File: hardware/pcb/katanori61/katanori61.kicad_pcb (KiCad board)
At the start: 4 copper layers, 82 x 37.4 mm, 59 parts, among them J1 XIAO RISER, J10 BAT (JST-PH), J13 USB-C, J2 OLED, J4 SPK IN, J5 SPK OUT, J6 BTN2, J7 REED+TOGGLE, K31 G6S-2F DC5, Q1 MMUN2133LT1G, Q2 AO3401A, Q31 SS8050, U1 TPS61090RSAR, U2 MCP73871-2CCI/ML, U3 INA226AIDGSR, U4 AS5600-ASOM

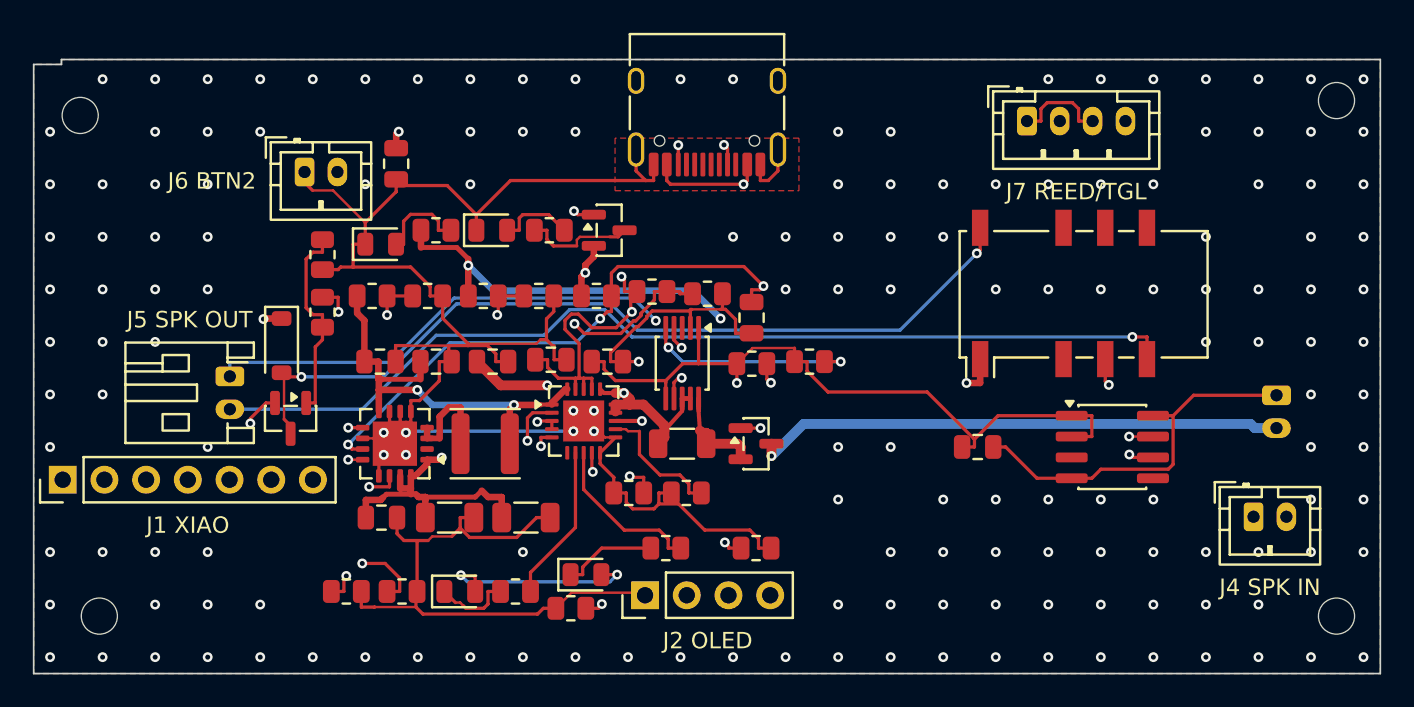
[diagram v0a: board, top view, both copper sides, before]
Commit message: pcb v6.1: R2・R6・R7 を 0603 へ／V5 を 0.8mm の独立した組へ／手はんだの GND にサーマル
外からの指摘 4 件のうち 1〜4 を直す。

1. 足形の食い違い
   Basic で選び直した R2(C23137)・R6(C22961)・R7(C23254) は 0603 なのに
   足形が 0805 のままだった。0805 のパッドの内側の間 0.875 に 0603 の胴 1.6 が
   両端 0.36 ずつ乗るだけで、機械実装で着かないか立つ。

3. V5 が内層を遠回り
   U1 → J1（XIAO）が 57.49mm、うち 57.3mm が In2.Cu。JLCPCB の 4 層は
   内層 0.5oz が既定なので、同じ幅でも抵抗が 2 倍になる。
   0.4mm → 0.8mm の独立した組にして 29.46mm・18.1mΩ（前 141.5mΩ）。
   0.3A で 5.4mV（前 42.5mV）。

4. 電池の道の数字が古い
   gen_pcb.py の「12mm・10mΩ」は J10 を板の真ん中に置いていたときの値。
   実測に入れ替え: J10→Q2 31.16mm/25.5mΩ、Q2→R41 2.18mm/1.8mΩ、
   R41→U2 3.63mm/3.0mΩ、計 36.97mm・30.3mΩ（1A で 30mV）。

2. GND ベタが全パッド直結
   4 層で In1 が全面 GND になり、手はんだの口は 3 層が足に直結してこてで
   温度が逃げる。HAND_SOLDER の貫通 GND だけ thermal relief にした
   （J1-2 / J2-1 / J6-1 / J7-2 / J7-4 / J10-1 の 6 本）。表面実装は直結のまま。
   細いパッドは spoke が 1 本しか立たないので katanori61.kicad_dru を生成し、
   貫通パッドだけ min_resolved_spokes 1 に緩める。

ついでに見つけた不具合
   pad_box() が部品の角度を足しておらず、270° 置きの U3 で縦横が入れ替わって
   いた。ケルビンの線の端が U3 のパッドの 0.335 外に落ちていたのを自動配線が
   繕っていた。
   fab.py の JLC_ROT に R_0603_1608Metric（2 本足・補正 0）を足した。
   gen_case_parts.py の「いまの手書きの表は 9 個」は表を生成に変えた時点で
   嘘になっていたので消した。

検算
   配線 708 本・貫通穴 59 個・未接続 0・回路図との差 0・DRC エラー 0
   （警告は留め穴 4 と USB-C のシルク 2 のみ。starved_thermal は 0）
   模型・STL・ガーバー・BOM・CPL を出し直した。
   レジンの sk_hub 12.02mm³ は以前からの当たり（HEAD で 12.59）。
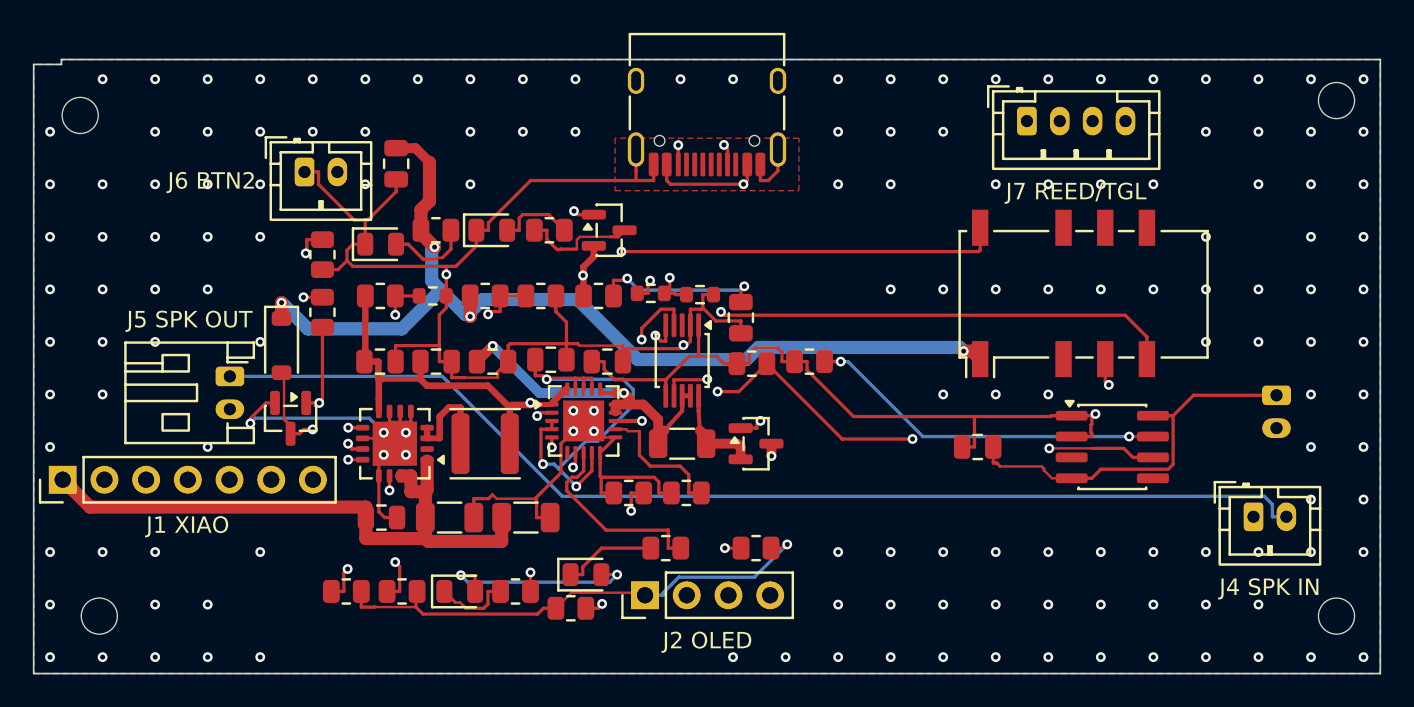
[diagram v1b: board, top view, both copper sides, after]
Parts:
- R2, R6, R7: footprint Resistor_SMD:R_0805_2012Metric -> Resistor_SMD:R_0603_1608Metric
- moved C32 0.65 mm to (83.1, 55.7)
- moved R1 0.50 mm to (61.1, 54.4)
- moved R7 0.46 mm to (80.6, 54.3)
- moved R2 0.31 mm to (64.3, 54.4)
- moved U3 0.16 mm to (79.5, 58.3)
- moved R6 0.13 mm to (77.6, 54.2)
- moved R13 0.12 mm to (74.4, 54.4)
- moved R4 0.12 mm to (70.9, 54.4)
- moved R3 0.12 mm to (67.5, 54.4)
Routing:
- net V33: track 96.2 -> 116.0 mm
- net SPKO: track 60.4 -> 72.3 mm
- net SDA: track 92.6 -> 103.5 mm, vias 3 -> 4
- net SCL: track 95.4 -> 87.5 mm
- net GND: track 305.8 -> 297.9 mm, vias 165 -> 156
- net EN: track 60.3 -> 68.0 mm
- net VPCC: track 21.4 -> 15.1 mm
- net BATG: track 17.2 -> 11.2 mm
- net COL: track 52.3 -> 57.9 mm
- net SPKM: track 73.6 -> 68.3 mm, vias 1 -> 0
- net BASE: track 12.2 -> 16.8 mm, vias 0 -> 2
- net STAT2: track 9.58 -> 13.4 mm, vias 0 -> 2
- net FB: track 20.7 -> 17.4 mm
- net BATRAW: track 32.4 -> 35.0 mm
- net VSYS: track 39.7 -> 37.2 mm, vias 3 -> 2
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
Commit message: pcb v6.1: FB を U1 の足元へ／リレーを AS5600 の横から退けた／長い幹を裏へ
指摘「昇圧の FB が遠い」を直す。板を見たら指摘どおりだった。
  R3 12.42mm / R4 14.32mm・FB はのべ 17.42mm でうち内層 13.21mm・ビア 2 個。
  内層の斜めの区間は L1 の枠を横切り、x 24.73 で FB が y 14.21・SW が y 14.33 ＝ 真下。
  In1 の GND の面は無事（廊下の 2mm 以内の穴 4 個のうち 3 個は GND 自身のビアで面を切らない）。

FB
  R3・R4 を U1 の 14 番の真下（Y 10.65）へ。V5 の出力コンデンサの列を 9.5 → 8.6 に下げて
  1.4mm の廊下を空けた（0805 のパッド 1.45 ＋ すきま 0.15×2 が入らなかったため）。
  ⇒ のべ 3.45mm・全部 F.Cu・ビア 0 個。

🔴 リレー K31 を AS5600 の横から退けた
  前は胴と胴が 3.16mm・芯と芯が 9.47mm で、しかも「筐体の仮置きから前へ 2.0」＝
  電磁石を、磁気で角度を読むセンサの真横へ限界まで寄せていた。
  MEDIATOR-V6-HANDOFF.md 3 章の「設計で潰す手は無い」は誤り。板の 64% には部品の胴が無く、
  留め穴・欠き・縁 0.5 を避けてもリレーが入る場所は 501 通りあった。
  90° 回して X 46.48〜57.18・Y 20.30〜35.60 へ。
    芯と芯 9.47 → 19.81mm（2.09 倍・双極子の場は 1/r³ なので約 9.2 分の 1）
    胴と胴 Y 3.16 → 4.05・X 0 → 6.57
  実機で確かめる項目（つまみを固定して K31 開／閉で AGC と RAW ANGLE を 2 読み）は残る。

長い幹を裏へ（自動配線に任せると内層 0.5oz へ逃げて抵抗が倍になる）
  🔴 2026-09-17 朝に書いた「J10 → Q2 31.16mm・25.5mΩ（B.Cu）」は私の誤り。層を見ずに
     長さだけで計算していた。実際は内層 In2 に 34.27mm で 56.6mΩ だった。
  bat_trunk() … J10 → Q2 を裏へ。56.6 → 26.7mΩ。
    ⚠ 最初 AS5600 の真裏を一直線に通したが、前の帯（Y 9.5）へ下ろした。+2.8mΩ 払って
      センサから 4.7mm 離す。磁気の見積もりは仮定の上の計算で、測った値ではないため。
  v5_trunk() … C6 の足元 → XIAO のライザーを裏へ。64.9 → 20.7mΩ。
  vlipo_link() … R41 → U2。自動配線が引けたり引けなかったりした谷を先に固定。
  R41・U3・Q2 を右へ 1.0。U2 の右の辺と R41 のあいだが 1.595mm しかなく、
  VLIPO 0.6 ＋ PROG1 0.2 ＋ PROG3 0.2 ＋ すきま 0.15×4 ＝ 1.6 に 0.005 足りなかった。

thermal relief の規則の置き場所を直した
  🔴 kicad-cli は katanori61.kicad_dru（カスタム規則）を読まない。わざと壊した規則を
     入れても素通りした。min_resolved_spokes は gen_sch.py が書く .kicad_pro に置く。
  ⇒ .kicad_dru の生成をやめ、ファイルを消した。

検算
  未接続 0・DRC エラー 0（警告は留め穴 4 と USB-C のシルク 2）
  すきまの下限 0.15 を下回る組 0 件（最小 0.152）
  筐体の当たり sk_hub は **レジンもナイロンも 0.00mm³**（以前から残っていたレジンの
  12.02mm³ も消えた）
  ⚠ 板の外は数えていない。電池に最初から付いている尻尾は 26AWG 80mm 往復で 20.6mΩ、
    28AWG なら 34.0mΩ あり、板の道より大きい。実物の線を測るのが先。
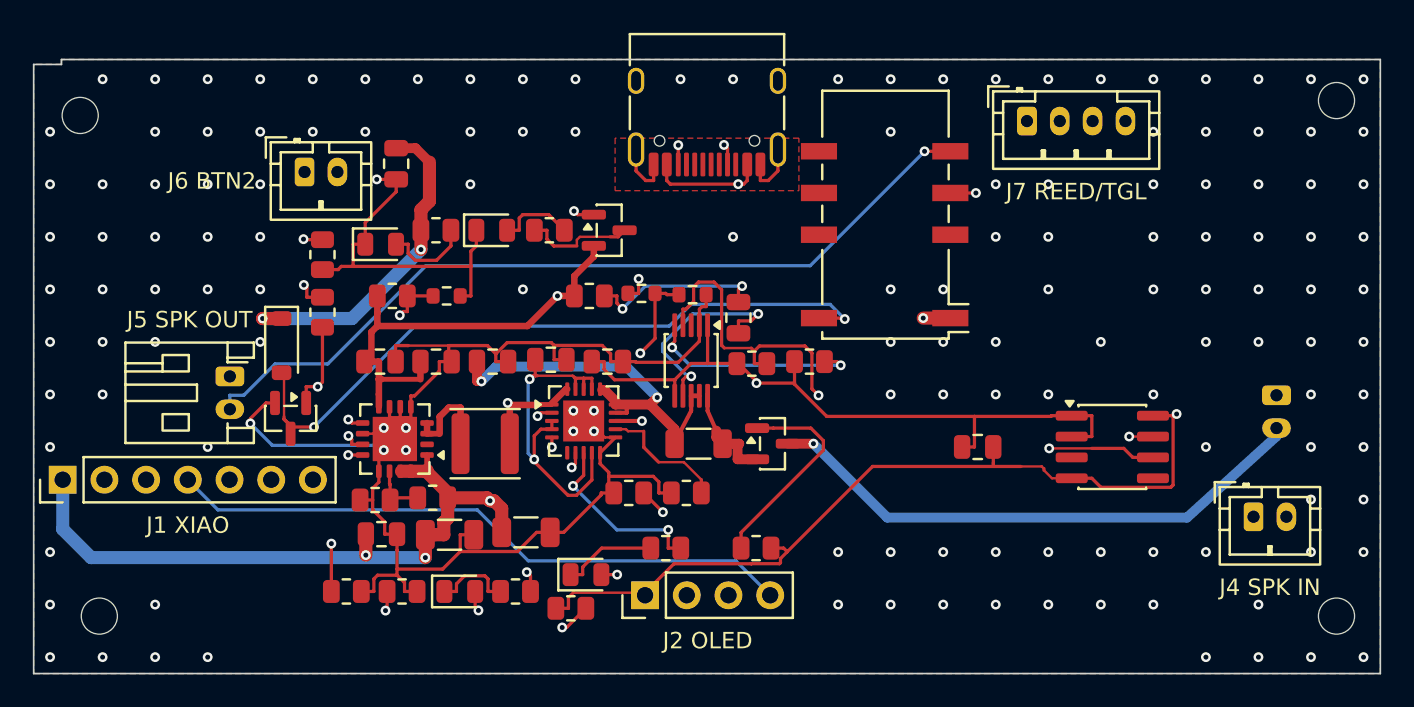
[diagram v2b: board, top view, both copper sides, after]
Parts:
- C4: renamed from C8; value 10uF -> 0.1uF
- C41: renamed from R43; value 10K -> 0.1uF; footprint Resistor_SMD:R_0805_2012Metric -> Capacitor_SMD:C_0805_2012Metric
- C7: renamed from C41; value 0.1uF -> 10uF
- C8: renamed from R42; value 10K -> 10uF; footprint Resistor_SMD:R_0805_2012Metric -> Capacitor_SMD:C_0805_2012Metric
- R16: renamed from C1; value 10uF -> 1.0K; footprint Capacitor_SMD:C_0805_2012Metric -> Resistor_SMD:R_0805_2012Metric
- R17: renamed from C4; value 0.1uF -> 100K; footprint Capacitor_SMD:C_0805_2012Metric -> Resistor_SMD:R_0805_2012Metric
- R2: renamed from R4; value 200K -> 330K; footprint Resistor_SMD:R_0805_2012Metric -> Resistor_SMD:R_0603_1608Metric
- R3: renamed from R17; value 100K -> 1.87M
- R4: renamed from R16; value 1.0K -> 200K
- R42: renamed from R1; value 1.87M -> 10K
- R43: renamed from R2; value 330K -> 10K; footprint Resistor_SMD:R_0603_1608Metric -> Resistor_SMD:R_0805_2012Metric
- moved R43 23.3 mm to (87.3, 58.4)
- moved R42 23.0 mm to (83.7, 58.5)
- moved R17 17.2 mm to (79.8, 66.4)
- moved R16 17.1 mm to (76.2, 66.4)
- moved R4 15.5 mm to (60.8, 66.8), turned to 180 degrees
- moved R3 15.5 mm to (64.3, 66.7), turned to 180 degrees
- moved K31 13.1 mm to (91.8, 49.4), turned to 180 degrees
- moved C41 12.3 mm to (74.9, 58.4)
- moved C8 12.2 mm to (71.5, 58.3)
- moved C4 6.99 mm to (64.5, 58.4)
- moved C7 6.99 mm to (68.0, 58.4)
- moved C1 6.86 mm to (61.1, 58.4)
- moved R2 5.73 mm to (65.2, 54.4)
- moved R1 5.66 mm to (61.8, 54.4)
- moved C6 1.05 mm to (65.3, 68.9)
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- renumbered C7 to C1, R3 to R1
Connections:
- C1 pad 1: VLIPO -> VSYS
- C4 pad 1: VBUS -> VSYS
- C41 pad 2: SCL -> GND
- C7 pad 1: V33 -> VLIPO
- C8 pad 1: V33 -> VBUS
- C8 pad 2: SDA -> GND
- R1 pad 1: V5 -> VSYS
- R1 pad 2: FB -> LBI
- R16 pad 1: VSYS -> GND
- R16 pad 2: GND -> PROG1
- R17 pad 1: VSYS -> GND
- R17 pad 2: GND -> PROG3
- R2 pad 1: FB -> LBI
- R3 pad 1: GND -> V5
- R3 pad 2: PROG3 -> FB
- R4 pad 1: GND -> FB
- R4 pad 2: PROG1 -> GND
- R42 pad 1: VSYS -> V33
- R42 pad 2: LBI -> SDA
- R43 pad 1: LBI -> V33
- R43 pad 2: GND -> SCL
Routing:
- net SPKM: track 68.3 -> 93.1 mm
- net SPKO: track 72.3 -> 50.9 mm
- net V33: track 116.0 -> 95.8 mm
- net SPKP: track 13.8 -> 28.8 mm
- net COL: track 57.9 -> 43.4 mm
- net FB: track 17.4 -> 3.45 mm, vias 2 -> 0
- net SDA: track 103.5 -> 90.2 mm, vias 4 -> 2
- net CC2: track 40.1 -> 46.4 mm
- net VSYS: track 37.2 -> 42.6 mm
- net V5: track 116.7 -> 112.0 mm, vias 4 -> 6
- net GND: track 297.9 -> 302.0 mm, vias 156 -> 148
- net VLIPO: track 21.4 -> 25.1 mm
- net STAT2: track 13.4 -> 9.77 mm
- net SCL: track 87.5 -> 91.1 mm
- net EN: track 68.0 -> 64.5 mm
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
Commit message: pcb v6.1: AS5600 のまわりを自動配線の立入禁止に／VBUS の幹とスピーカー 3 本を太らせる
別スレッドの発注前レビュー 2 件を、こちらで測り直して一致を確認したうえで直した。

🔒 ユーザー 2026-09-17「AS5600 付近に極太線通すのやめませんかね」「バンバン通るんですけど」
  幅を決める組を足すたびに、自動配線がセンサの周りへ太い線を呼び込んでいた。
  直す前の実測（胴 X 63.75〜67.65 / Y 11.35〜16.25 からの距離）:
    SPKP 0.6mm  **0.00mm（真下）**   ← 0.44A rms の交流
    SPKM 0.6mm  1.39mm
    BATRAW 0.6mm 1.85mm              ← 今日私が通した線
  測って安心するのをやめ、置けなくした。
    dsn.py … 立入禁止を層ごとに指定できるようにした（5 つ目に層の組）
    gen_pcb.py … U4 のまわり X 60.2〜71.2 / Y 7.8〜19.8 を In2.Cu と B.Cu で立入禁止。
      表（F.Cu）は塞がない。U4 の SDA・SCL・V33 が出られなくなるため。
    bat_trunk() … その外を回る道へ引き直し（東の帯 X 72.0 → 前の帯 Y 6.5）
  直した後: 胴から 12mm 以内の 0.4mm 以上の線は最短 **4.62mm**。真下を通る線は無い。

1. VBUS の幹（vbus_trunk）
  幅を決める組に入れていなかったので、幹まで 0.2mm で内層へ逃げていた。
    J13 → U2.18  **102.5 → 28.6mΩ**（B.Cu 0.6mm で J13 → C8 だけ先に引いて protect）
  C8 → U2 の枝は 0.2mm のまま。U2 の 0.25mm のパッドに 0.6mm は押し込めない。
  MCP73871 はリニア充電なので VBUS ＝ 充電電流 ＋ 機体の電流で、実測ベース 0.78A・
  設計上限 1.22A。内層 0.2mm の許容は約 0.37A しかなかった。

2. スピーカーの 3 本（SPK_NETS 0.6mm）
    SPKP  137.6 → **49.8mΩ**
    SPKO  125.0 → **74.6mΩ**
    SPKM  457.5 → **83.2mΩ**（のべ 93.1 → 71.1mm）
    合計  720 → **208mΩ**。8Ω に対して 8.3% → **2.5%**
  ⚠ POWER.md 560 行の「2 極目で両切り」は実装していない。理由は下。

docs/POWER.md 560 行の 🔒 を外した
  「ミュートリレーの 2 極目は、接点 1 つが溶着してもスピーカーの回路が切れる形にする」は
  出どころが無い。入ったのは c9d74b6（2026-09-13 21:40「決まった事を一覧にする」）で、
  そのコミットの文自身が「ユーザー『絵がでてきません。終わってる』で中断」と書いている。
  この章の他の 🔒 は必ず日付と発言を引いているが、この 1 行だけ無い。
  🔒 ユーザー 2026-09-17「そんなの書いた覚えがない」→ ⬜ 未決に落とし、経緯を併記して残した。

ついでに
  R3・R4 を左右へ 0.6 ずつ（21.0/24.1 → 20.4/24.7）。2 つの FB のパッドの間が 0.22mm しか
  なく、U1 の V5（15・16 番）が真下へ降りられずに浮いていた。いまは隙間 1.42mm。
  check_sch_voice.py が build/ に網表を置き去りにしていたのを、読んだら消す形にした
  （check_sch.py と同じ）。9/15 の死んだ網表が別セッションに読まれて誤解された。

検算
  未接続 0・DRC エラー 0（警告は留め穴 4 と USB-C のシルク 2）
  すきまの下限 0.15 を下回る組 0 件（最小 0.152）／回路図との差 0 件／穴と外形の照合 合致
  筐体の当たり sk_hub レジン 0.00・ナイロン 0.00
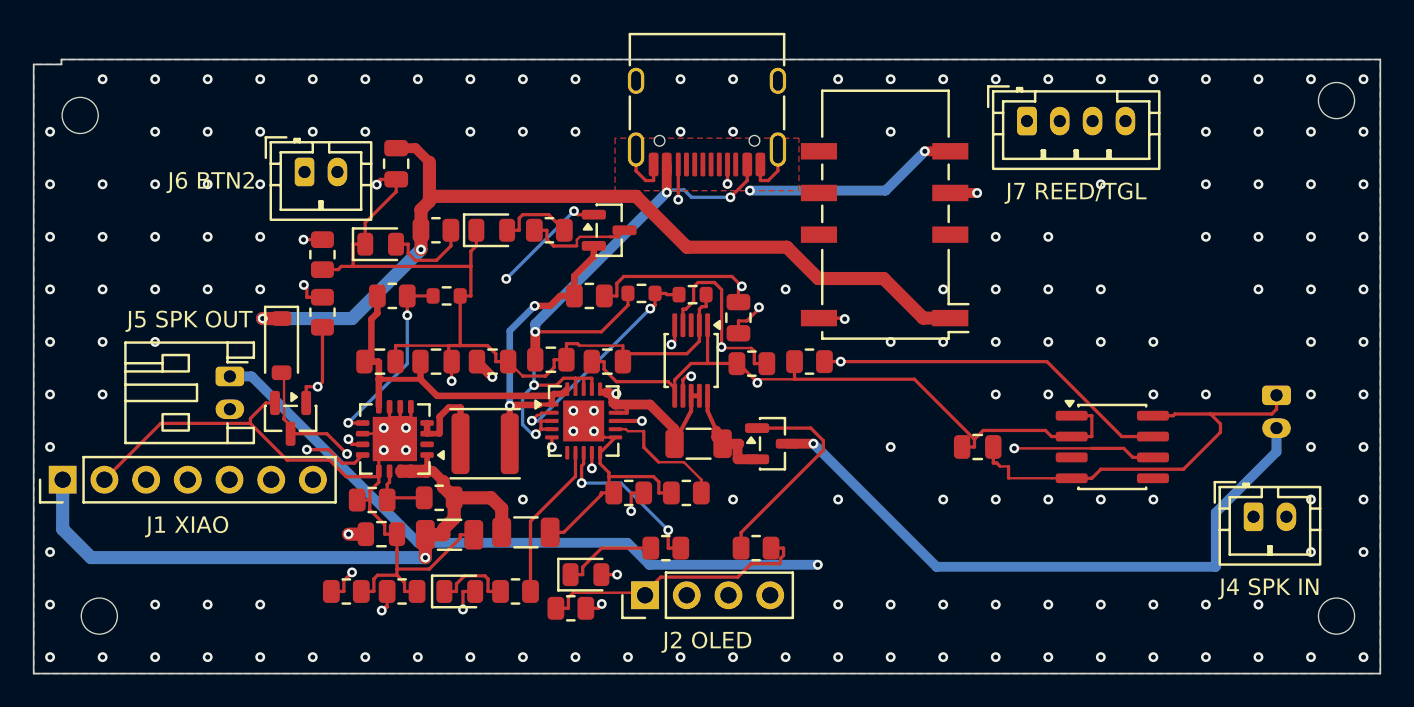
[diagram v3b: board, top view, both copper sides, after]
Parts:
- moved R3 0.39 mm to (64.7, 66.7)
- moved R4 0.18 mm to (60.6, 66.8)
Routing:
- net SPKM: track 93.1 -> 71.1 mm, vias 0 -> 1
- net SCL: track 91.1 -> 83.9 mm, vias 3 -> 2
- net IN: track 13.9 -> 21.0 mm
- net V5: track 112.0 -> 118.4 mm, vias 6 -> 4
- net LBO: track 22.7 -> 28.1 mm, vias 2 -> 3
- net BATRAW: track 34.0 -> 39.2 mm
- net SDA: track 90.2 -> 95.0 mm
- net GND: track 302.0 -> 306.4 mm, vias 148 -> 160
- net BTN: track 20.9 -> 25.3 mm
- net VLIPO: track 25.1 -> 21.0 mm
- net EN: track 64.5 -> 68.2 mm, vias 3 -> 2
- net VSYS: track 42.6 -> 39.3 mm
- net CC2: track 46.4 -> 43.3 mm
- net SPKP: track 28.8 -> 31.2 mm
- net VBUS: track 71.8 -> 70.3 mm, vias 6 -> 8
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
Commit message: pcb v6.1: VBUS の最後の枝を太く（C8 を U2 の入力ピンの真上へ）／電源のコンデンサの横に GND の穴
発注前レビューで出た 1 件。幹（J13 → C8）は 0.6mm にしてあったが、C8 → U2 の 18・19 番は
「3mm の枝」のつもりで自動配線任せで、板を測ると B.Cu 0.2mm × 3.3mm → 穴 → F.Cu 0.2mm × 2.7mm
＋ ピンの足 0.66 ＝ 6.6mm・16mΩ。太くした幹（15.2mm・12.5mΩ）より大きかった。
原因は線幅ではなく配置:
  ・C8 が横向きで、2 番（GND）の下端と U2 のピン列のあいだが 0.66mm
  ・C8 の 2 番が乗る表の GND の島に穴が無く、GND の 0.2mm 線が C8 の 1 番の真下を横切る

直し:
  ・C8 を縦（90°）にして 1 番を U2 の 17〜19 番（3 本とも VBUS）の真上へ。1 番 → ピンは 1.2mm
    隣の 20 番（VSYS）・16 番（VLIPO）まで 0.275 ずつ。幹は 1 番の左の横で表へ上がる
  ・C41 34.0 → 36.4・R13 23.0 → 23.5（C8 の置き場と GND の穴の分）
  ・cap_gnd_vias(): C8・C6・C9・C1 の GND パッドの横に GND の穴（📄 TPS61090 12.1）
    C2 は置ける側が無いので外した（下は V5 の幹・上は R4 の FB まで 0.18・右は C6 の V5 まで 0.15）
  ・check_pre(): 先に引いた穴 × 別ネットの先に引いた線。最初の置き方で GND の穴が裏の
    VBUS の幹と V5 の幹に乗った（protect どうしなので DRC まで出ない短絡）。生成で止める

結果（板から測った値・外層 1oz）: J13 → U2 の入力 28.5 → 13.4mΩ・全区間 0.6mm 以上・穴 2 個。
DRC エラー 0・未接続 0（警告は前からの 6 件）。check_pcb 0 件（最小 VSYS ↔ LBO 0.151）。
check_sch 0 件。check_fab 合わない所なし。ガーバー・BOM・CPL・v61_parts を出し直した。
⚠ 筐体側の当たり検査（case_v6_1.scad）は回していない。動いたのは背 0.45〜1.25 の 0805 が 3 個。

古い記述の片付け:
  ・CHECK_PADS の Q2 が 1.0 古く、生成のたびに警告が 3 行出ていた（向きは合っていた）
  ・gen_pcb.py 頭の「J10 → Q2 28.6mm 23.9mΩ」→ 37.6mm 32mΩ（AS5600 をよけて回す前の値だった）
  ・PCB-V61.md 4.1 のシルク 0.12 の ⬜（ガーバーは表裏とも 0.150 だけ）・5 章に --incremental の件
  ・gen_sch.py の J13 の注記（1.53 出し → 1.3）
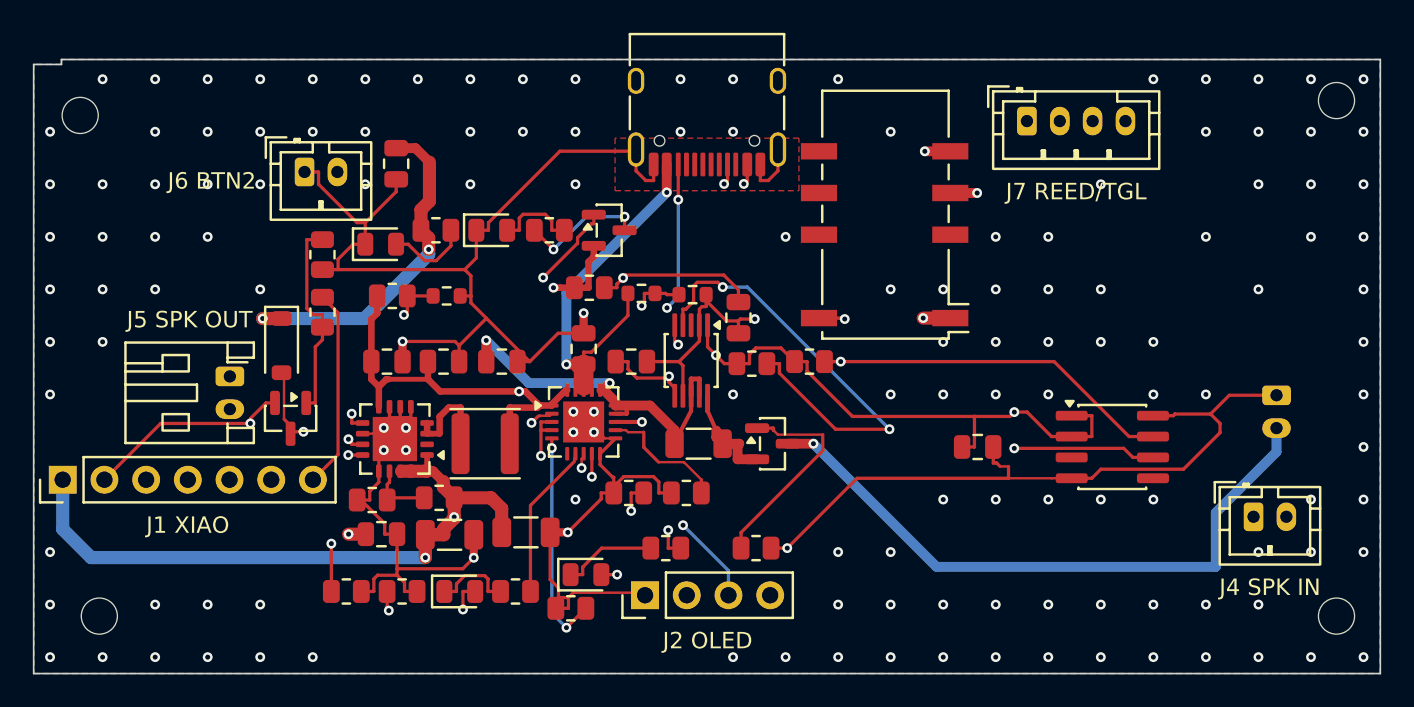
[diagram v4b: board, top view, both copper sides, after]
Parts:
- moved C8 2.10 mm to (73.5, 57.6), turned to 90 degrees
- moved C41 1.46 mm to (76.4, 58.4)
- moved C7 0.57 mm to (68.5, 58.4)
- moved R13 0.50 mm to (73.8, 53.9)
- moved C4 0.46 mm to (65.0, 58.4)
- moved C1 0.42 mm to (61.5, 58.4)
- moved U2 0.06 mm to (73.5, 62.1)
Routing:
- net GND: track 306.4 -> 281.4 mm, vias 160 -> 146
- net SPKM: track 71.1 -> 92.4 mm, vias 1 -> 0
- net BTN: track 25.3 -> 43.6 mm
- net CC1: track 42.6 -> 56.4 mm
- net V33: track 95.8 -> 108.7 mm, vias 1 -> 3
- net IN: track 21.0 -> 12.1 mm, vias 1 -> 0
- net COL: track 43.4 -> 48.0 mm
- net LBO: track 28.1 -> 24.4 mm, vias 3 -> 2
- net VBUS: track 70.3 -> 74.0 mm, vias 8 -> 7
- net BASE: track 15.9 -> 12.4 mm, vias 2 -> 0
- net CC2: track 43.3 -> 39.8 mm, vias 2 -> 3
- net SDA: track 95.0 -> 98.2 mm, vias 2 -> 3
- net V5: track 118.4 -> 121.2 mm, vias 4 -> 6
- net VPCC: track 14.1 -> 16.7 mm
- net VLIPO: track 21.0 -> 23.6 mm
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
